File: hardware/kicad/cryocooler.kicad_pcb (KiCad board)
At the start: 4 copper layers, 130 x 100 mm, 288 parts, among them J1 USB_C, J10 RTD PT1000 4-wire, J11 AMP OUT (+ / -), J12 CRYOCOOLER (+ / -), J13 COMPRESSOR RELAY / GND, J2 12V IN, J3 FAN (4-pin PWM), J4 PUMP (4-pin PWM), J5 ALPHACOOL ES FLOW (3-pin), J6 ALPHACOOL ES NTC 10k, J7 PANEL BUTTON, J8 AMP REM / GND, J9 AMP SIGNAL IN / GND, Q1 IRF4905S, Q2 BSS138, Q3 BSS138, Q4 BSS138, Q5 BSS138, Q6 BSS84, Q7 BSS138, Q8 BSS84, SW1 RESET, SW2 BOOT, SW3 POWER, U1 ESP32-S3-WROOM-2-N32R16V, U10 EMC2303-x-KP, U11 LTC2954CTS8-2, U12 LM4040DBZ-5, U13 CL25N8-G, U14 ADS1220IPW, U15 AP63205WU-7, U16 LD1117S33TR, U17 ISO7741DW, U18 ACS37800KMACTR-030B3-SPI, U19 LSM6DSOXTR, U2 USBLC6-2SC6, U20 ADP5071AREZ, U21 ADP7142AUJZ, U22 ADP7182AUJZ, U23 INA239AIDGSR, U24 74AHCT1G125, U25 SC18IS604PW, U26 74LVC1G125, U3 SG-8002CA-PH 25MHz, U4 AD9833BRMZ, U5 OPA1656ID, U6 AD633JRZ-R7, U7 MCP4921-E/SN, U8 LM4040DBZ-2.5, U9 OPA188ID

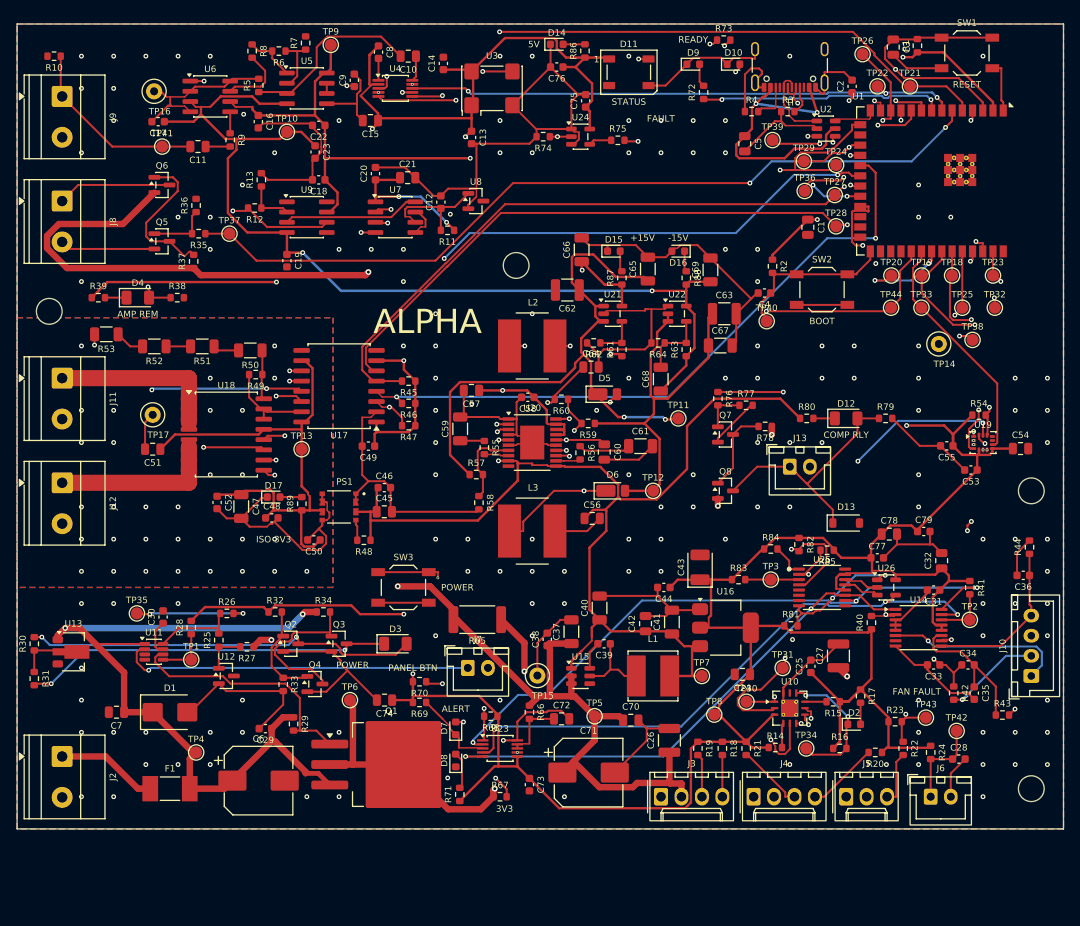
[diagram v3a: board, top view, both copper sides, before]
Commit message: Move the IMU off-board (J14) and add labelled module boxes to the PCB
The LSM6DSOX is now the Adafruit breakout (product 4438) mounted on the
cryocooler and cabled to a 10-pin JST XH header (J14) over the shared SPI
bus. U19 and its capacitors are gone; J14 and six 100 R series resistors
are added, and every other reference number is unchanged.

PCB (130 x 110 mm, was 130 x 100):
- one outlined, labelled silkscreen box per module (pcbfloorplan.py); the
  placer keeps parts inside their box and reserves a label pocket beside
  every part so each label sits next to its own part
- box 3D models for U3, L2, L3, F1 and PS1, whose library models are missing
- re-routed; DRC 0 errors, 0 unconnected; back logo recentred
- gen_pcb.py texts redoes the silkscreen on a routed board

Firmware: SPI clock constant for the module, comments updated; ambient
temperature now reads the cooler-body IMU temperature.

Docs, BOM and fabrication files regenerated.

Co-Authored-By: Claude Sonnet 5.5 <noreply@anthropic.com>
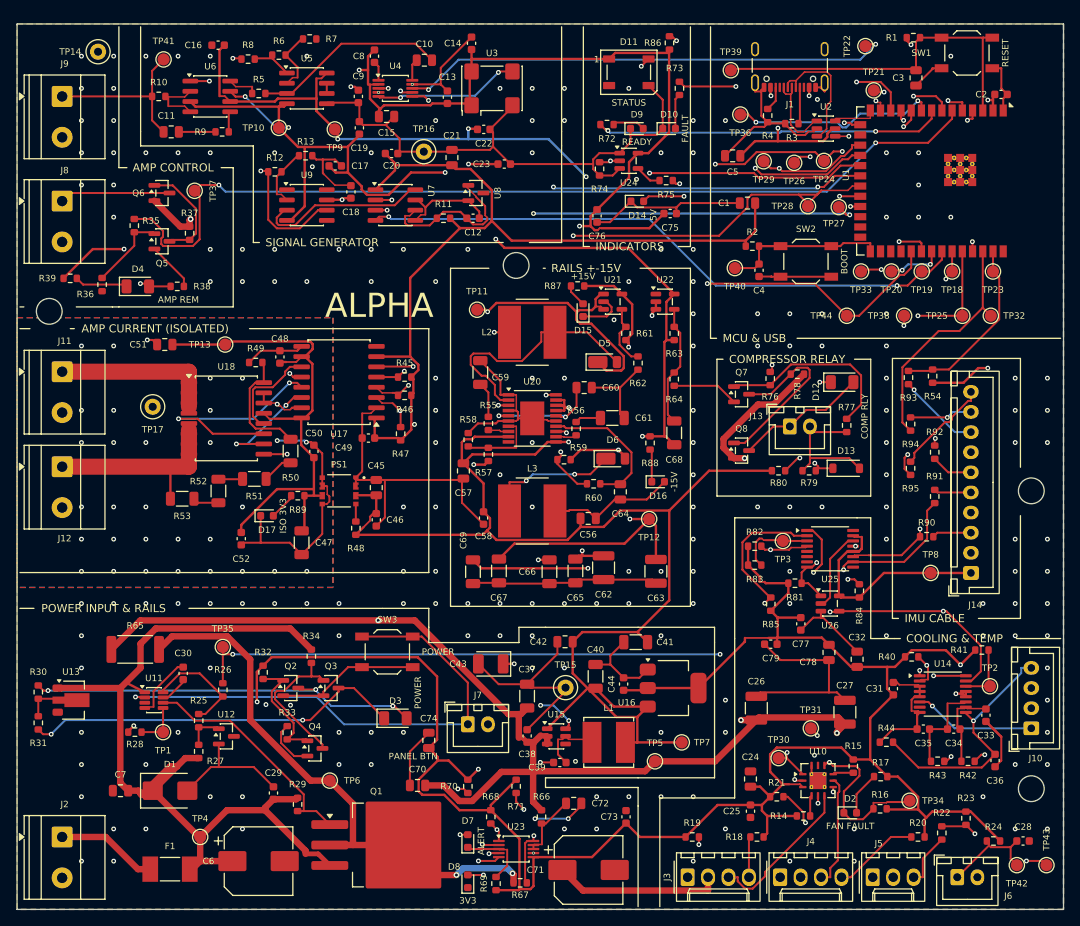
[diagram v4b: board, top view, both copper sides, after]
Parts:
- removed C53, C55: 100nF, C_0603_1608Metric
- removed C54: 10uF, C_0805_2012Metric
- removed U19: LSM6DSOXTR, LGA-14_3x2.5mm_P0.5mm_LayoutBorder3x4y
- added J14: IMU LSM6DSOX module, JST_XH_B10B-XH-A_1x10_P2.50mm_Vertical, F.Cu at (118.5, 68.2)
- added R90: 100, R_0603_1608Metric, F.Cu at (113.0, 63.7)
- added R91: 100, R_0603_1608Metric, F.Cu at (114.0, 58.7)
- added R92: 100, R_0603_1608Metric, F.Cu at (114.0, 53.2)
- added R93: 100, R_0603_1608Metric, F.Cu at (110.7, 43.9)
- added R94: 100, R_0603_1608Metric, F.Cu at (111.0, 49.7)
- added R95: 100, R_0603_1608Metric, F.Cu at (111.0, 55.2)
- moved TP14 110.6 mm to (10.1, 3.45)
- moved C69 47.7 mm to (56.6, 68.0), turned to -90 degrees
- moved R65 42.7 mm to (14.7, 77.7)
- moved C66 40.2 mm to (66.1, 68.0), turned to -90 degrees
- moved C67 39.2 mm to (59.9, 68.0), turned to -90 degrees
- moved C65 38.6 mm to (69.4, 68.0), turned to -90 degrees
- moved C62 34.8 mm to (72.9, 67.5), turned to -90 degrees
- moved TP16 34.3 mm to (50.5, 15.9)
- moved C63 33.1 mm to (79.4, 68.0), turned to -90 degrees
- moved TP8 32.1 mm to (113.5, 68.2)
- moved R44 30.0 mm to (108.0, 89.2), turned to 180 degrees
- moved D16 28.8 mm to (79.6, 56.9), turned to 0 degrees
- moved C43 28.6 mm to (58.9, 79.5), turned to 180 degrees
- moved TP11 28.4 mm to (57.1, 35.5)
- moved C70 27.7 mm to (49.8, 94.6), turned to 180 degrees
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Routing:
- net +3V3: track 491.7 -> 572.0 mm, vias 9 -> 10
- net +12V: track 274.4 -> 326.7 mm
- net +15V: track 96.3 -> 144.8 mm, vias 3 -> 6
- net FLOW_TACH: track 83.5 -> 118.4 mm, vias 2 -> 3
- net +5V: track 309.3 -> 341.4 mm
- net -15V: track 126.5 -> 157.8 mm, vias 2 -> 5
- net SPI_MOSI: track 228.0 -> 257.1 mm, vias 7 -> 6
- net SPI_SCK: track 224.8 -> 249.0 mm, vias 7 -> 6
- net Net-(D14-A): track 2.71 -> 26.2 mm, vias 0 -> 2
- net Net-(Q7-G): track 5.35 -> 23.6 mm
- net SCL: track 31.2 -> 48.4 mm, vias 2 -> 3
- net -16V5: track 48.9 -> 65.9 mm, vias 0 -> 3
- net SDA: track 25.0 -> 41.3 mm, vias 2 -> 3
- net INA239_CS: track 105.1 -> 119.6 mm, vias 2 -> 4
- net AMP_REM_EN: track 102.6 -> 116.9 mm
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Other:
- board size 130 x 100 mm -> 130 x 110 mm
- board text added: "AMP CONTROL"
- board text added: "AMP CURRENT (ISOLATED)"
- board text added: "COMPRESSOR RELAY"
- board text added: "COOLING & TEMP"
- board text added: "IMU CABLE"
- board text added: "INDICATORS"
- board text added: "MCU & USB"
- board text added: "POWER INPUT & RAILS"
- board text added: "RAILS +-15V"
- board text added: "SIGNAL GENERATOR"
